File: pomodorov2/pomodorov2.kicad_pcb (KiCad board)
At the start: 2 copper layers, 14.3 x 38.4 mm, 26 parts, among them J1 USB_B_Micro, J2 TC2050-IDC, J3 Conn_01x08, U1 MDBT50Q-1MV2, Y1 32.768kHz, Y1 32MHz, Y2 32.768kHz

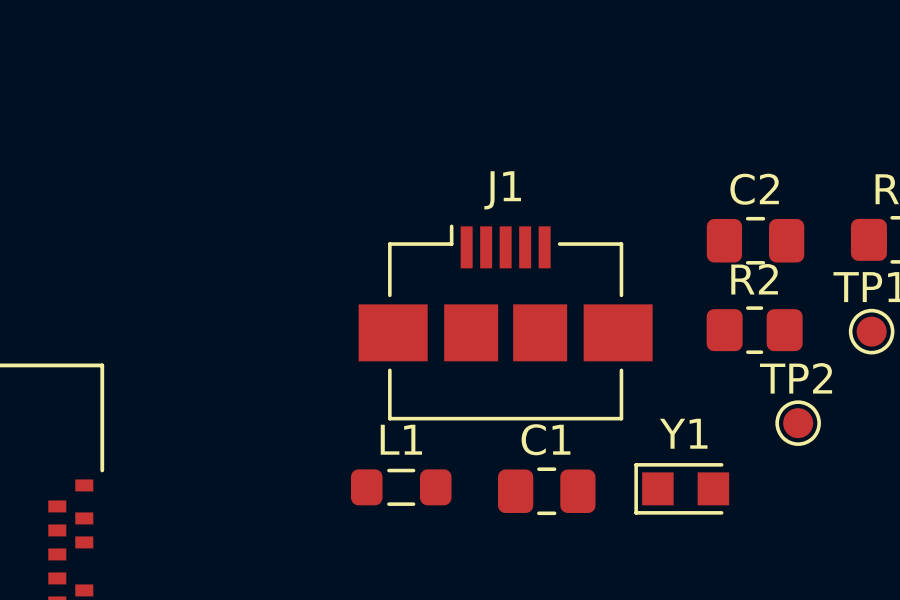
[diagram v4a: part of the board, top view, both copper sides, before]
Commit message: Make schematic more legible 👓
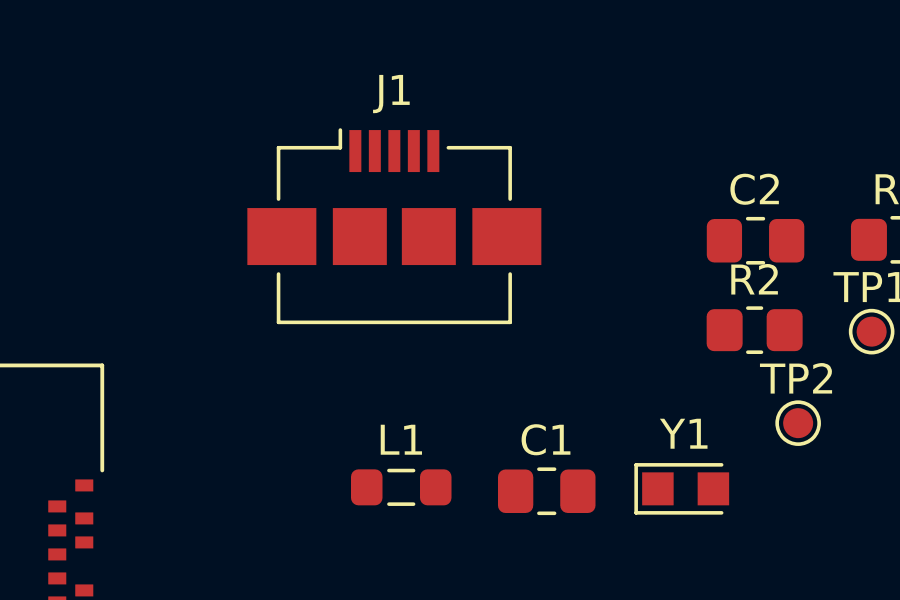
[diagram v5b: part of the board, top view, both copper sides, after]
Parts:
- moved J1 4.91 mm to (140.7, 86.5)
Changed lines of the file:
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@@
     (fp_line (start -0.261252 -0.735) (end 0.261252 -0.735) (layer "F.SilkS") (width 0.12))
     (fp_line (start -0.261252 0.735) (end 0.261252 0.735) (layer "F.SilkS") (width 0.12))
-    (fp_line (start 1.88 -0.98) (end 1.88 0.98) (layer "F.CrtYd") (width 0.05))
     (fp_line (start -1.88 0.98) (end -1.88 -0.98) (layer "F.CrtYd") (width 0.05))
     (fp_line (start 1.88 0.98) (end -1.88 0.98) (layer "F.CrtYd") (width 0.05))
     (fp_line (start -1.88 -0.98) (end 1.88 -0.98) (layer "F.CrtYd") (width 0.05))
-    (fp_line (start -1 -0.625) (end 1 -0.625) (layer "F.Fab") (width 0.1))
+    (fp_line (start 1.88 -0.98) (end 1.88 0.98) (layer "F.CrtYd") (width 0.05))
     (fp_line (start 1 -0.625) (end 1 0.625) (layer "F.Fab") (width 0.1))
     (fp_line (start -1 0.625) (end -1 -0.625) (layer "F.Fab") (width 0.1))
+    (fp_line (start -1 -0.625) (end 1 -0.625) (layer "F.Fab") (width 0.1))
     (fp_line (start 1 0.625) (end -1 0.625) (layer "F.Fab") (width 0.1))
     (pad "1" smd roundrect (at -1.0375 0) (size 1.175 1.45) (layers "F.Cu" "F.Paste" "F.Mask") (roundrect_rratio 0.212766)
@@
   )
   (footprint "Connector_USB:USB_Micro-B_Amphenol_10104110_Horizontal" (layer "F.Cu")
-    (at 144.426 89.686)
+    (at 140.716 86.476)
     (descr "USB Micro-B, horizontal, https://cdn.amphenol-icc.com/media/wysiwyg/files/drawing/10104110.pdf")
     (tags "USB Micro B horizontal")
@@
     (fp_line (start -0.261252 0.735) (end 0.261252 0.735) (layer "F.SilkS") (width 0.12))
     (fp_line (start -0.261252 -0.735) (end 0.261252 -0.735) (layer "F.SilkS") (width 0.12))
+    (fp_line (start 1.88 0.98) (end -1.88 0.98) (layer "F.CrtYd") (width 0.05))
     (fp_line (start -1.88 -0.98) (end 1.88 -0.98) (layer "F.CrtYd") (width 0.05))
+    (fp_line (start -1.88 0.98) (end -1.88 -0.98) (layer "F.CrtYd") (width 0.05))
     (fp_line (start 1.88 -0.98) (end 1.88 0.98) (layer "F.CrtYd") (width 0.05))
-    (fp_line (start 1.88 0.98) (end -1.88 0.98) (layer "F.CrtYd") (width 0.05))
-    (fp_line (start -1.88 0.98) (end -1.88 -0.98) (layer "F.CrtYd") (width 0.05))
+    (fp_line (start -1 0.625) (end -1 -0.625) (layer "F.Fab") (width 0.1))
+    (fp_line (start -1 -0.625) (end 1 -0.625) (layer "F.Fab") (width 0.1))
+    (fp_line (start 1 -0.625) (end 1 0.625) (layer "F.Fab") (width 0.1))
     (fp_line (start 1 0.625) (end -1 0.625) (layer "F.Fab") (width 0.1))
-    (fp_line (start -1 -0.625) (end 1 -0.625) (layer "F.Fab") (width 0.1))
-    (fp_line (start -1 0.625) (end -1 -0.625) (layer "F.Fab") (width 0.1))
-    (fp_line (start 1 -0.625) (end 1 0.625) (layer "F.Fab") (width 0.1))
     (pad "1" smd roundrect (at -1.0375 0) (size 1.175 1.45) (layers "F.Cu" "F.Paste" "F.Mask") (roundrect_rratio 0.212766)
       (net 2 "GND") (pintype "passive"))
@@
       (effects (font (size 1 1) (thickness 0.15)))
     )
+    (fp_line (start -5.25 -4.25) (end -5.25 -7.75) (layer "F.SilkS") (width 0.127))
+    (fp_line (start 5.25 -7.75) (end 5.25 -4.25) (layer "F.SilkS") (width 0.127))
     (fp_line (start -5.25 4.2) (end -5.25 6.55) (layer "F.SilkS") (width 0.127))
-    (fp_line (start -5.25 -4.25) (end -5.25 -7.75) (layer "F.SilkS") (width 0.127))
     (fp_line (start -5.25 -7.75) (end 5.25 -7.75) (layer "F.SilkS") (width 0.127))
-    (fp_line (start 5.25 -7.75) (end 5.25 -4.25) (layer "F.SilkS") (width 0.127))
     (fp_circle (center -5.75 -3.75) (end -5.65 -3.75) (layer "F.SilkS") (width 0.2) (fill none))
-    (fp_line (start -5.5 8) (end -5.5 -3.95) (layer "F.CrtYd") (width 0.05))
     (fp_line (start 6.2 -8) (end 6.2 -3.95) (layer "F.CrtYd") (width 0.05))
     (fp_line (start 5.5 -3.95) (end 5.5 8) (layer "F.CrtYd") (width 0.05))
+    (fp_line (start 5.5 8) (end -5.5 8) (layer "F.CrtYd") (width 0.05))
     (fp_line (start -6.2 -8) (end 6.2 -8) (layer "F.CrtYd") (width 0.05))
     (fp_line (start 6.2 -3.95) (end 5.5 -3.95) (layer "F.CrtYd") (width 0.05))
-    (fp_line (start 5.5 8) (end -5.5 8) (layer "F.CrtYd") (width 0.05))
     (fp_line (start -6.2 -3.95) (end -6.2 -8) (layer "F.CrtYd") (width 0.05))
+    (fp_line (start -5.5 8) (end -5.5 -3.95) (layer "F.CrtYd") (width 0.05))
     (fp_line (start -5.5 -3.95) (end -6.2 -3.95) (layer "F.CrtYd") (width 0.05))
     (fp_line (start -5.25 7.75) (end -5.25 -7.75) (layer "F.Fab") (width 0.127))
@@
     (pad "61" smd rect locked (at 2 0.55) (size 0.4 0.6) (layers "F.Cu" "F.Paste" "F.Mask")
       (net 79 "unconnected-(U1-Pad61)") (pinfunction "P1.01") (pintype "bidirectional"))
-    (zone (net 0) (net_name "") (layers *.Cu) (hatch full 0.508)
+    (zone (net 0) (net_name "") (layer "F.Cu") (hatch full 0.508)
       (connect_pads (clearance 0))
       (min_thickness 0.01)
-      (keepout (tracks allowed) (vias not_allowed) (pads allowed ) (copperpour allowed) (footprints allowed))
+      (keepout (tracks not_allowed) (vias not_allowed) (pads not_allowed ) (copperpour not_allowed) (footprints allowed))
+      (fill (thermal_gap 0.508) (thermal_bridge_width 0.508))
+      (polygon
+        (pts
+          (xy 119.53 92.072)
+          (xy 131.93 92.072)
+          (xy 131.93 95.872)
+          (xy 119.53 95.872)
+        )
+      )
+    )
+    (zone (net 0) (net_name "") (layer "F.Cu") (hatch full 0.508)
+      (connect_pads (clearance 0))
+      (min_thickness 0.01)
+      (keepout (tracks not_allowed) (vias not_allowed) (pads not_allowed ) (copperpour not_allowed) (footprints allowed))
       (fill (thermal_gap 0.508) (thermal_bridge_width 0.508))
       (polygon
@@
       (polygon
         (pts
+          (xy 123.43 95.872)
+          (xy 125.03 95.872)
+          (xy 125.03 97.072)
+          (xy 123.43 97.072)
+        )
+      )
+    )
+    (zone (net 0) (net_name "") (layers *.Cu) (hatch full 0.508)
+      (connect_pads (clearance 0))
+      (min_thickness 0.01)
+      (keepout (tracks allowed) (vias not_allowed) (pads allowed ) (copperpour allowed) (footprints allowed))
+      (fill (thermal_gap 0.508) (thermal_bridge_width 0.508))
+      (polygon
+        (pts
           (xy 119.53 92.072)
           (xy 131.93 92.072)
@@
         )
       )
-    )
-    (zone (net 0) (net_name "") (layer "F.Cu") (hatch full 0.508)
-      (connect_pads (clearance 0))
-      (min_thickness 0.01)
-      (keepout (tracks not_allowed) (vias not_allowed) (pads not_allowed ) (copperpour not_allowed) (footprints allowed))
-      (fill (thermal_gap 0.508) (thermal_bridge_width 0.508))
-      (polygon
-        (pts
-          (xy 119.53 92.072)
-          (xy 131.93 92.072)
-          (xy 131.93 95.872)
-          (xy 119.53 95.872)
-        )
-      )
-    )
-    (zone (net 0) (net_name "") (layer "F.Cu") (hatch full 0.508)
-      (connect_pads (clearance 0))
-      (min_thickness 0.01)
-      (keepout (tracks not_allowed) (vias not_allowed) (pads not_allowed ) (copperpour not_allowed) (footprints allowed))
-      (fill (thermal_gap 0.508) (thermal_bridge_width 0.508))
-      (polygon
-        (pts
-          (xy 123.43 95.872)
-          (xy 125.03 95.872)
-          (xy 125.03 97.072)
-          (xy 123.43 97.072)
-        )
-      )

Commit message: A little routing and schematic cleanup 🧹
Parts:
- J3: value Conn_01x08 -> SOICbite
- moved TP2 64.9 mm to (90.5, 106.5)
- moved R1 64.7 mm to (95.2, 105.2), turned to 90 degrees
- moved R2 61.4 mm to (93.0, 105.2), turned to -90 degrees
- moved TP1 60.6 mm to (98.0, 106.2)
- moved J1 52.3 mm to (94.4, 110.7)
- moved R1 45.0 mm to (116.5, 107.0), turned to 0 degrees
- moved C2 43.3 mm to (109.8, 93.2), turned to 180 degrees
- moved Y1 40.9 mm to (109.6, 95.5)
- moved J3 39.5 mm to (117.2, 113.0), turned to 0 degrees
- moved L1 36.0 mm to (105.0, 95.5)
- moved C1 32.8 mm to (113.0, 94.5), turned to 90 degrees
- moved U1 19.7 mm to (106.8, 105.2), turned to 180 degrees
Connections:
- R1 pad 2: /USBD+ -> USBD+
- R2 pad 1: /USBD- -> USBD-
- U1 pad 34: unconnected-(U1-Pad34) -> USBD-
- U1 pad 35: unconnected-(U1-Pad35) -> USBD+
- U1 pad 40: unconnected-(U1-Pad40) -> ~RESET
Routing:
- net USBD-: track 0.00 -> 11.2 mm
- net USBD+: track 0.00 -> 8.65 mm
- net Net-(J1-Pad3): track 0.00 -> 6.04 mm
- net Net-(J1-Pad2): track 0.00 -> 5.85 mm
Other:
- board outline removed

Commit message: Some layout, schematic work 👷‍♂️
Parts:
- moved J2 74.9 mm to (94.0, 96.2), turned to 90 degrees
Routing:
- net SWCLK: track 0.07 -> 16.8 mm, vias 0 -> 2
- net SWDIO: track 0.13 -> 13.6 mm
- net USBD-: track 11.2 -> 0.00 mm
- net USBD+: track 8.65 -> 0.25 mm
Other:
- board outline added: 32.8 x 23.8 mm

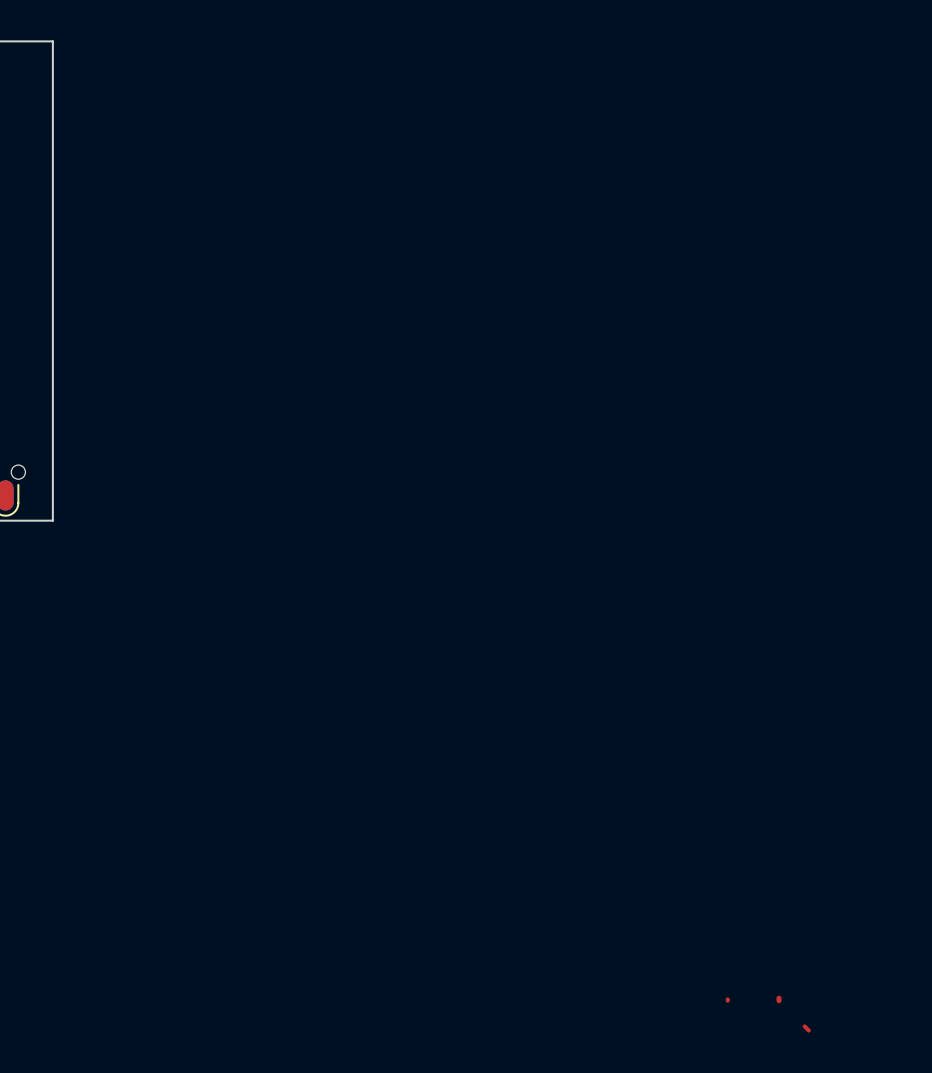
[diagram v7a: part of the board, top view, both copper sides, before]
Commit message: Add Stemma connector, add signals 📶
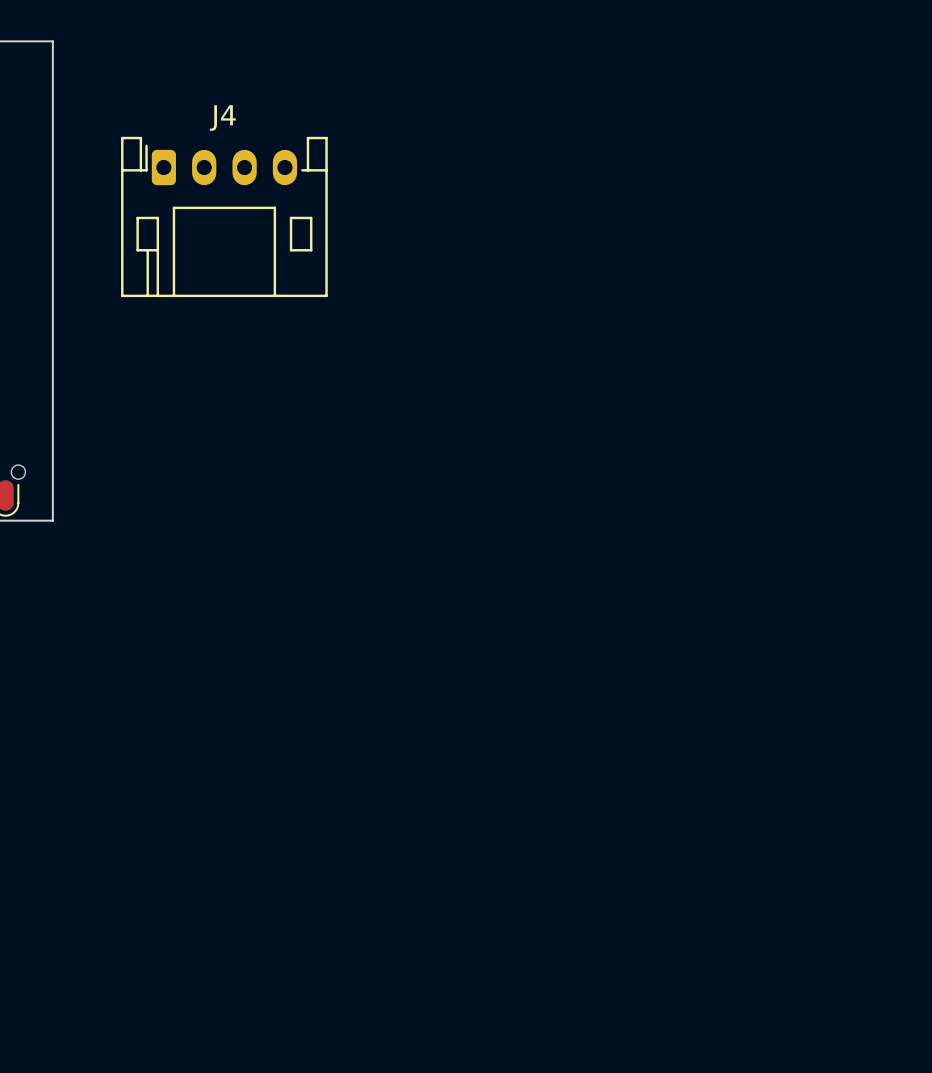
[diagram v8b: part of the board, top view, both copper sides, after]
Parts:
- added J4: Stemma, Connector_JST:JST_PH_S4B-PH-K_1x04_P2.00mm_Horizontal, F.Cu at (127.0, 96.0)
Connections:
- net SWCLK renamed /SWCLK
- net USBD+ renamed /USBD+
- net USBD- renamed /USBD-
- net ~RESET renamed /~RESET
- J2 pad 2: SWDIO -> /SWDIO
- J2 pad 6: SWO -> /SWO
- J3 pad 5: SWDIO -> /SWDIO
- J3 pad 6: SWO -> /SWO
- U1 pad 27: unconnected-(U1-Pad27) -> /SCL
- U1 pad 29: unconnected-(U1-Pad29) -> /SDA
- U1 pad 36: unconnected-(U1-Pad36) -> /SCK
- U1 pad 37: unconnected-(U1-Pad37) -> /MOSI
- U1 pad 39: unconnected-(U1-Pad39) -> /MISO
- U1 pad 47: unconnected-(U1-Pad47) -> /SWO
- U1 pad 48: unconnected-(U1-Pad48) -> /RXD
- U1 pad 49: unconnected-(U1-Pad49) -> /TXD
- U1 pad 51: SWDIO -> /SWDIO
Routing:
- net SWDIO: track 13.6 -> 0.00 mm
- net /SWDIO: track 0.00 -> 13.5 mm
